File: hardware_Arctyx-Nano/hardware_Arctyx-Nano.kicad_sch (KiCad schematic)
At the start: 70 parts, among them J1 USB_C_Receptacle_USB2.0_16P, J2 Conn_01x20_Pin, J3 Conn_01x20_Pin, SW1 SW_Push, U1 ICE40UP5K-SG48ITR, U2 RP2350A-QFN60, U3 W25Q128JVP, U4 RT8075ZQW, U5 TJ-S1608SW6TDSLCCYRGB-A5, Y1 Crystal_GND24

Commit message: production files generation and branding
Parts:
- R11: value 51k -> 100k
- R12: value R -> 22k
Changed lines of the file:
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@@
 	(wire
 		(pts
+			(xy 139.7 140.97) (xy 148.59 140.97)
+		)
+		(stroke
+			(width 0)
+			(type default)
+		)
+	)
+	(wire
+		(pts
 			(xy 330.2 152.4) (xy 330.2 156.21)
 		)
@@
 	(wire
 		(pts
-			(xy 139.7 140.97) (xy 148.59 140.97)
-		)
-		(stroke
-			(width 0)
-			(type default)
-		)
-	)
-	(wire
-		(pts
 			(xy 308.61 130.81) (xy 293.37 130.81)
 		)
@@
 	(wire
 		(pts
+			(xy 139.7 148.59) (xy 148.59 148.59)
+		)
+		(stroke
+			(width 0)
+			(type default)
+		)
+	)
+	(wire
+		(pts
 			(xy 231.14 95.25) (xy 219.71 95.25)
 		)
@@
 	(wire
 		(pts
-			(xy 139.7 148.59) (xy 148.59 148.59)
-		)
-		(stroke
-			(width 0)
-			(type default)
-		)
-	)
-	(wire
-		(pts
 			(xy 196.85 102.87) (xy 204.47 102.87)
 		)
@@
 	(global_label "1v2"
 		(shape input)
-		(at 139.7 140.97 90)
+		(at 144.78 140.97 90)
 		(fields_autoplaced yes)
 		(effects
@@
 		)
 		(property "Intersheetrefs" "${INTERSHEET_REFS}"
-			(at 139.7 134.5982 90)
+			(at 144.78 134.5982 90)
 			(effects
 				(font
@@
 	(global_label "GND"
 		(shape input)
-		(at 139.7 148.59 270)
+		(at 143.51 148.59 270)
 		(fields_autoplaced yes)
 		(effects
@@
 		)
 		(property "Intersheetrefs" "${INTERSHEET_REFS}"
-			(at 139.7 155.4457 90)
+			(at 143.51 155.4457 90)
 			(effects
 				(font
@@
 			)
 		)
-		(property "Value" "51k"
+		(property "Value" "100k"
 			(at 125.73 219.964 90)
 			(effects
@@
 			)
 		)
-		(property "Value" "R"
+		(property "Value" "22k"
 			(at 104.14 230.124 90)
 			(effects

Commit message: BOM Optimisation
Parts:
- C1, C2: value 15p -> 18p
- D1, D2, D3, D4, D5, D6: footprint LED_SMD:LED_0402_1005Metric -> LED_SMD:LED_0603_1608Metric
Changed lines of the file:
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@@
 			)
 		)
-		(property "Value" "15p"
+		(property "Value" "18p"
 			(at 198.12 126.9999 0)
 			(effects
@@
 			)
 		)
-		(property "Footprint" "LED_SMD:LED_0402_1005Metric"
+		(property "Footprint" "LED_SMD:LED_0603_1608Metric"
 			(at 36.83 144.78 0)
 			(effects
@@
 			)
 		)
-		(property "Footprint" "LED_SMD:LED_0402_1005Metric"
+		(property "Footprint" "LED_SMD:LED_0603_1608Metric"
 			(at 326.39 156.21 0)
 			(effects
@@
 			)
 		)
-		(property "Footprint" "LED_SMD:LED_0402_1005Metric"
+		(property "Footprint" "LED_SMD:LED_0603_1608Metric"
 			(at 36.83 134.62 0)
 			(effects
@@
 			)
 		)
-		(property "Footprint" "LED_SMD:LED_0402_1005Metric"
+		(property "Footprint" "LED_SMD:LED_0603_1608Metric"
 			(at 326.39 152.4 0)
 			(effects
@@
 			)
 		)
-		(property "Footprint" "LED_SMD:LED_0402_1005Metric"
+		(property "Footprint" "LED_SMD:LED_0603_1608Metric"
 			(at 36.83 139.7 0)
 			(effects
@@
 			)
 		)
-		(property "Footprint" "LED_SMD:LED_0402_1005Metric"
+		(property "Footprint" "LED_SMD:LED_0603_1608Metric"
 			(at 36.83 149.86 0)
 			(effects
@@
 			)
 		)
-		(property "Value" "15p"
+		(property "Value" "18p"
 			(at 198.12 142.2399 0)
 			(effects

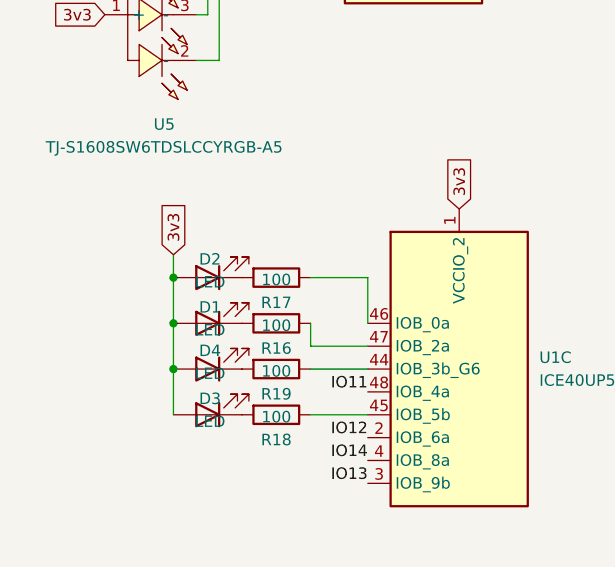
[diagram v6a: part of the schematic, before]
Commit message: Fix LED reference
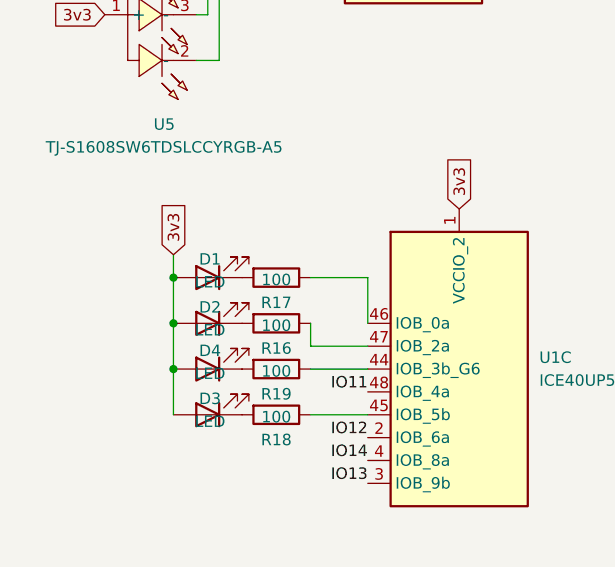
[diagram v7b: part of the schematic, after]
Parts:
- renumbered D2 to D1, D1 to D2
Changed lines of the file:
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@@
 		(on_board yes)
 		(dnp no)
-		(property "Reference" "D2"
+		(property "Reference" "D1"
 			(at 37.084 132.588 0)
 			(effects
@@
 			(project "hardware_Arctyx-Nano"
 				(path "/dadf11aa-8e96-42b0-bb48-2980919511bd"
-					(reference "D2")
+					(reference "D1")
 					(unit 1)
 				)
@@
 		(on_board yes)
 		(dnp no)
-		(property "Reference" "D1"
+		(property "Reference" "D2"
 			(at 37.084 137.922 0)
 			(effects
@@
 			(project ""
 				(path "/dadf11aa-8e96-42b0-bb48-2980919511bd"
-					(reference "D1")
-					(unit 1)
-				)
+					(reference "D2")
+					(unit 1)
+				)

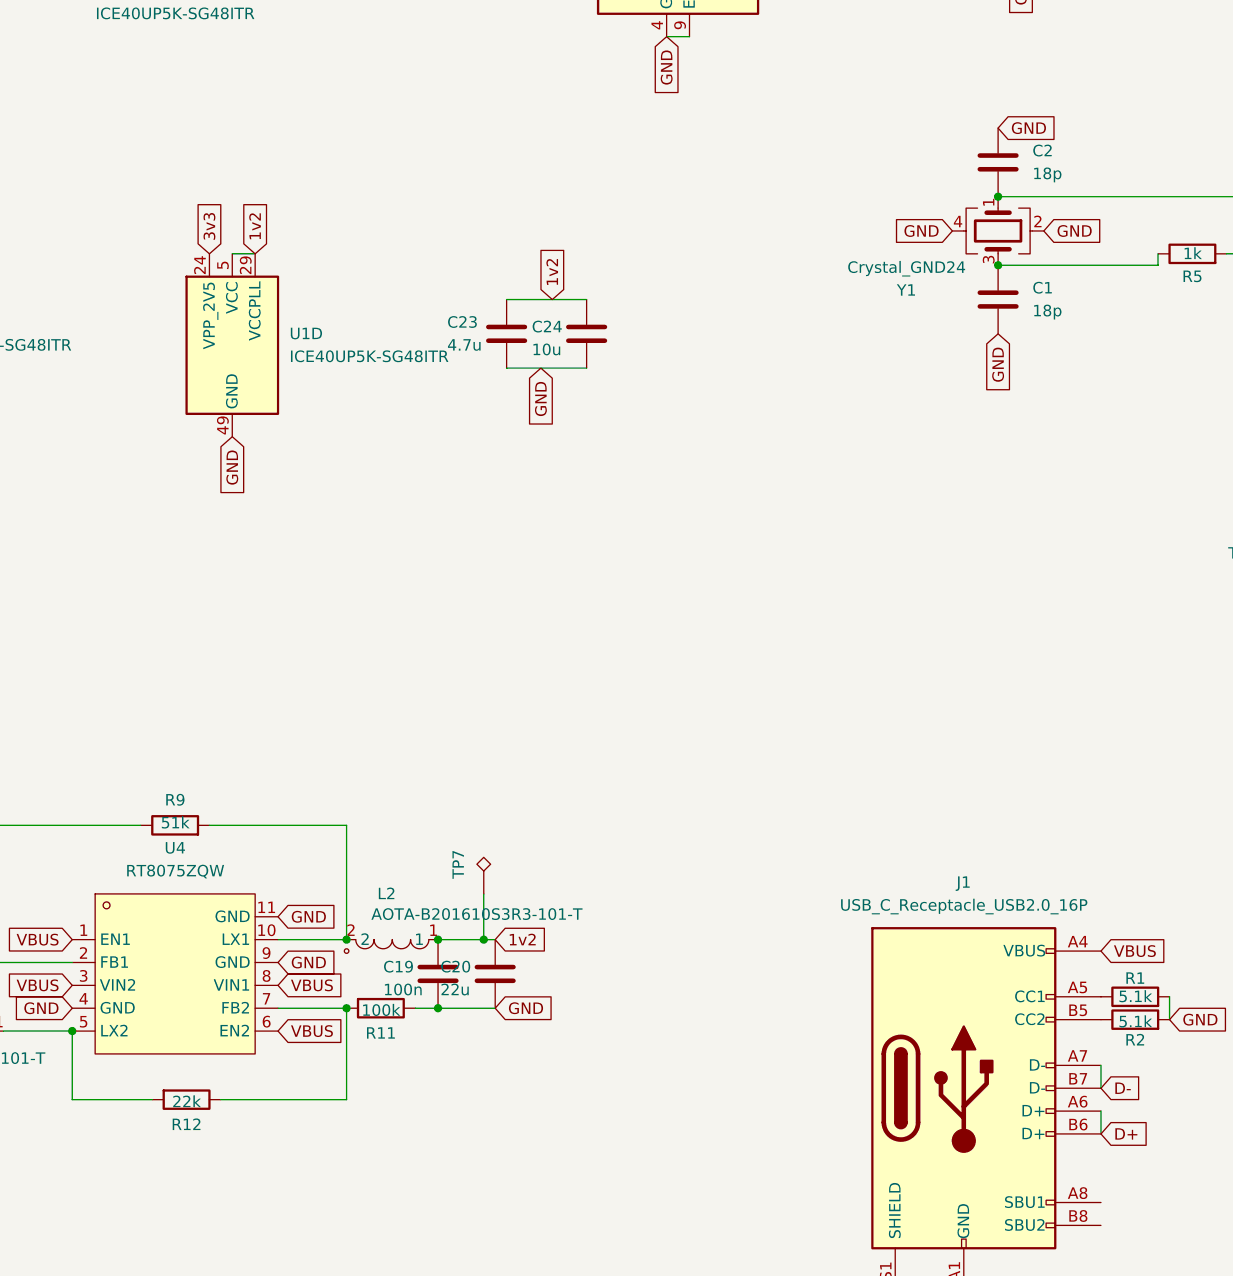
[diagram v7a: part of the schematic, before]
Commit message: update load capacitor values
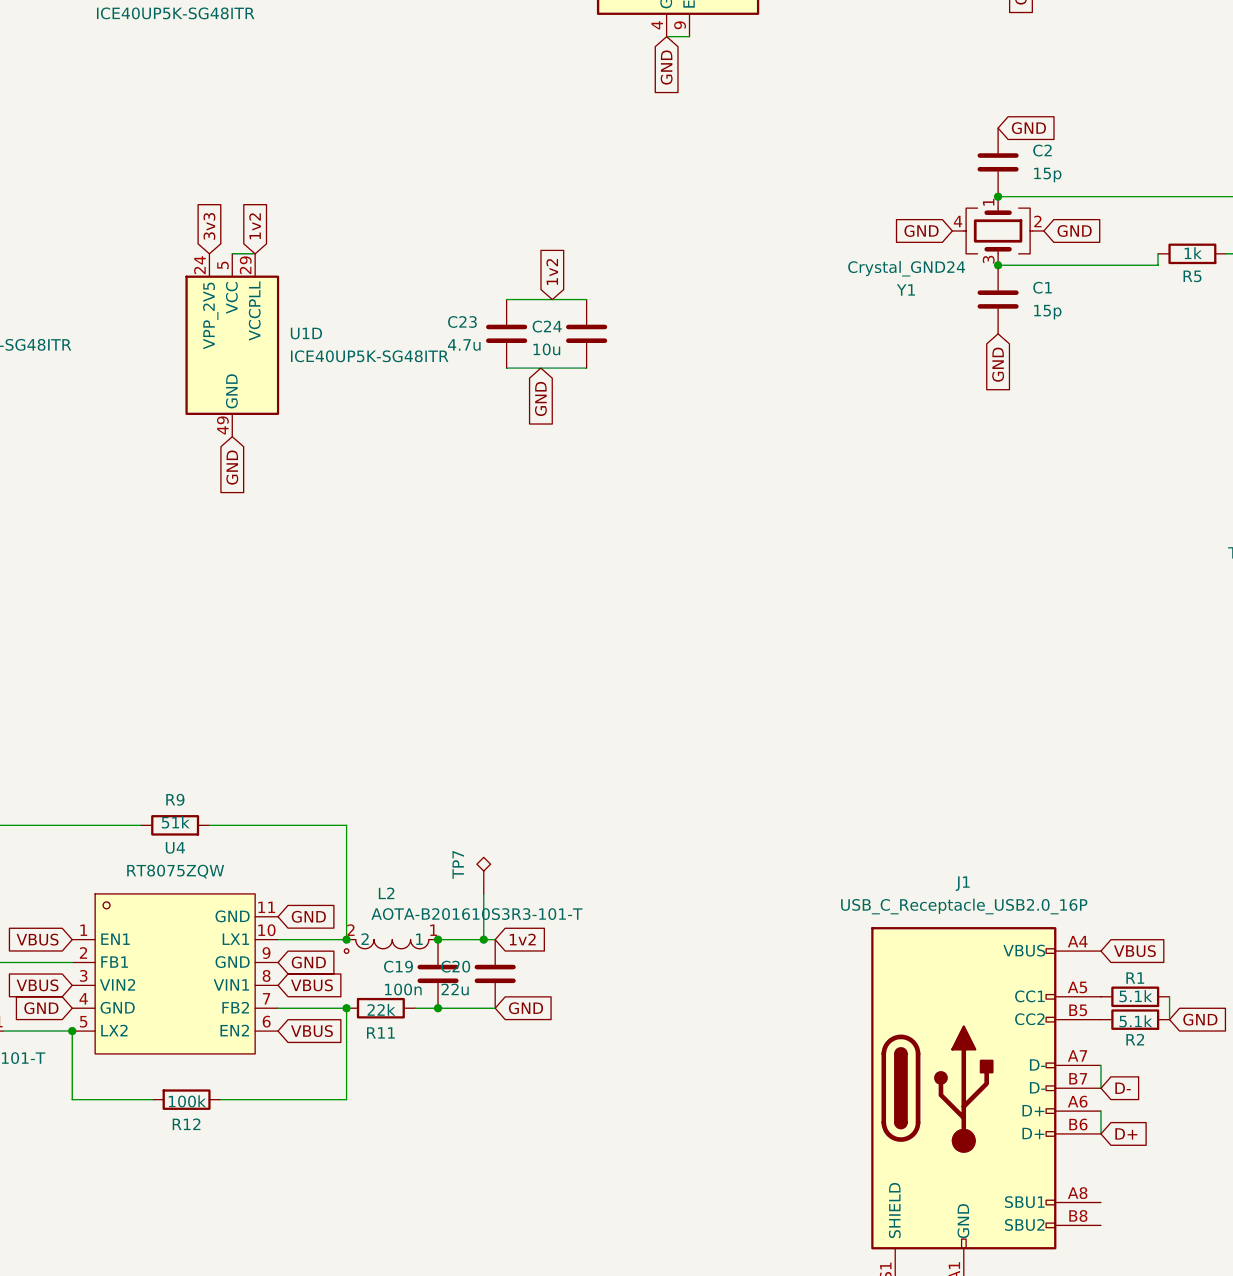
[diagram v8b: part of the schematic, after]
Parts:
- C1, C2: value 18p -> 15p
- R11: value 100k -> 22k
- R12: value 22k -> 100k
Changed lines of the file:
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@@
 			)
 		)
-		(property "Value" "18p"
+		(property "Value" "15p"
 			(at 198.12 126.9999 0)
 			(effects
@@
 			)
 		)
-		(property "Value" "100k"
+		(property "Value" "22k"
 			(at 125.73 219.964 90)
 			(effects
@@
 			)
 		)
-		(property "Value" "22k"
+		(property "Value" "100k"
 			(at 104.14 230.124 90)
 			(effects
@@
 			)
 		)
-		(property "Value" "18p"
+		(property "Value" "15p"
 			(at 198.12 142.2399 0)
 			(effects
